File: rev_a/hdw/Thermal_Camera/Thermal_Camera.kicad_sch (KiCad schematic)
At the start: 0 parts

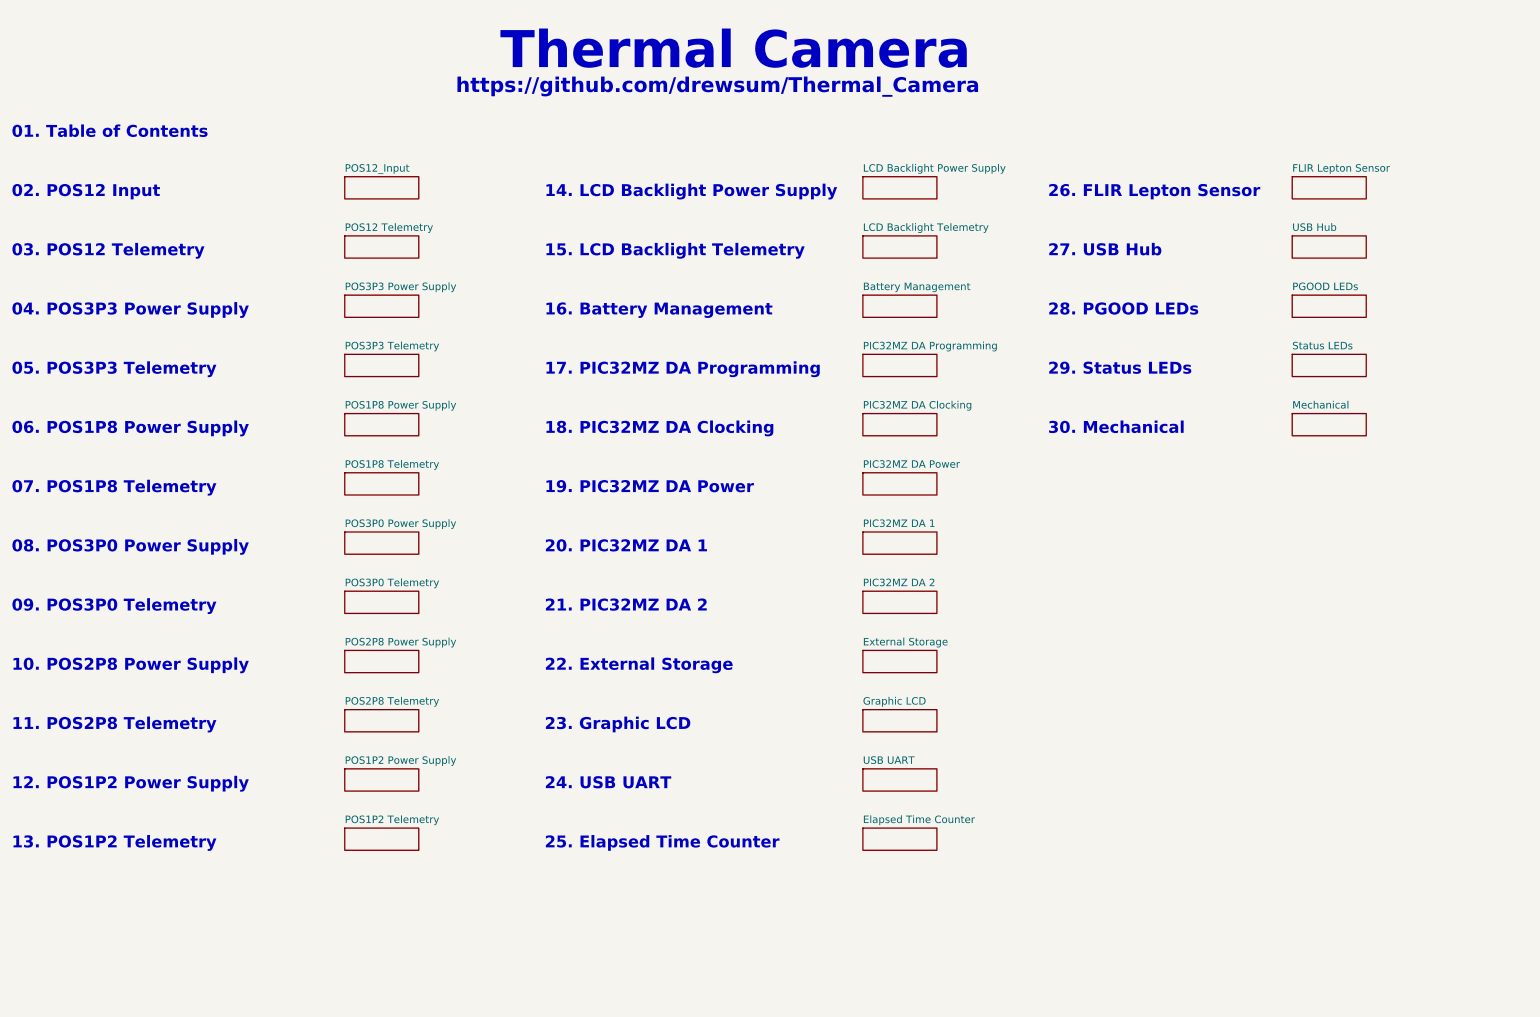
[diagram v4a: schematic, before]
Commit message: changed a lot of circuits from +3.3V to +3.0V VDD
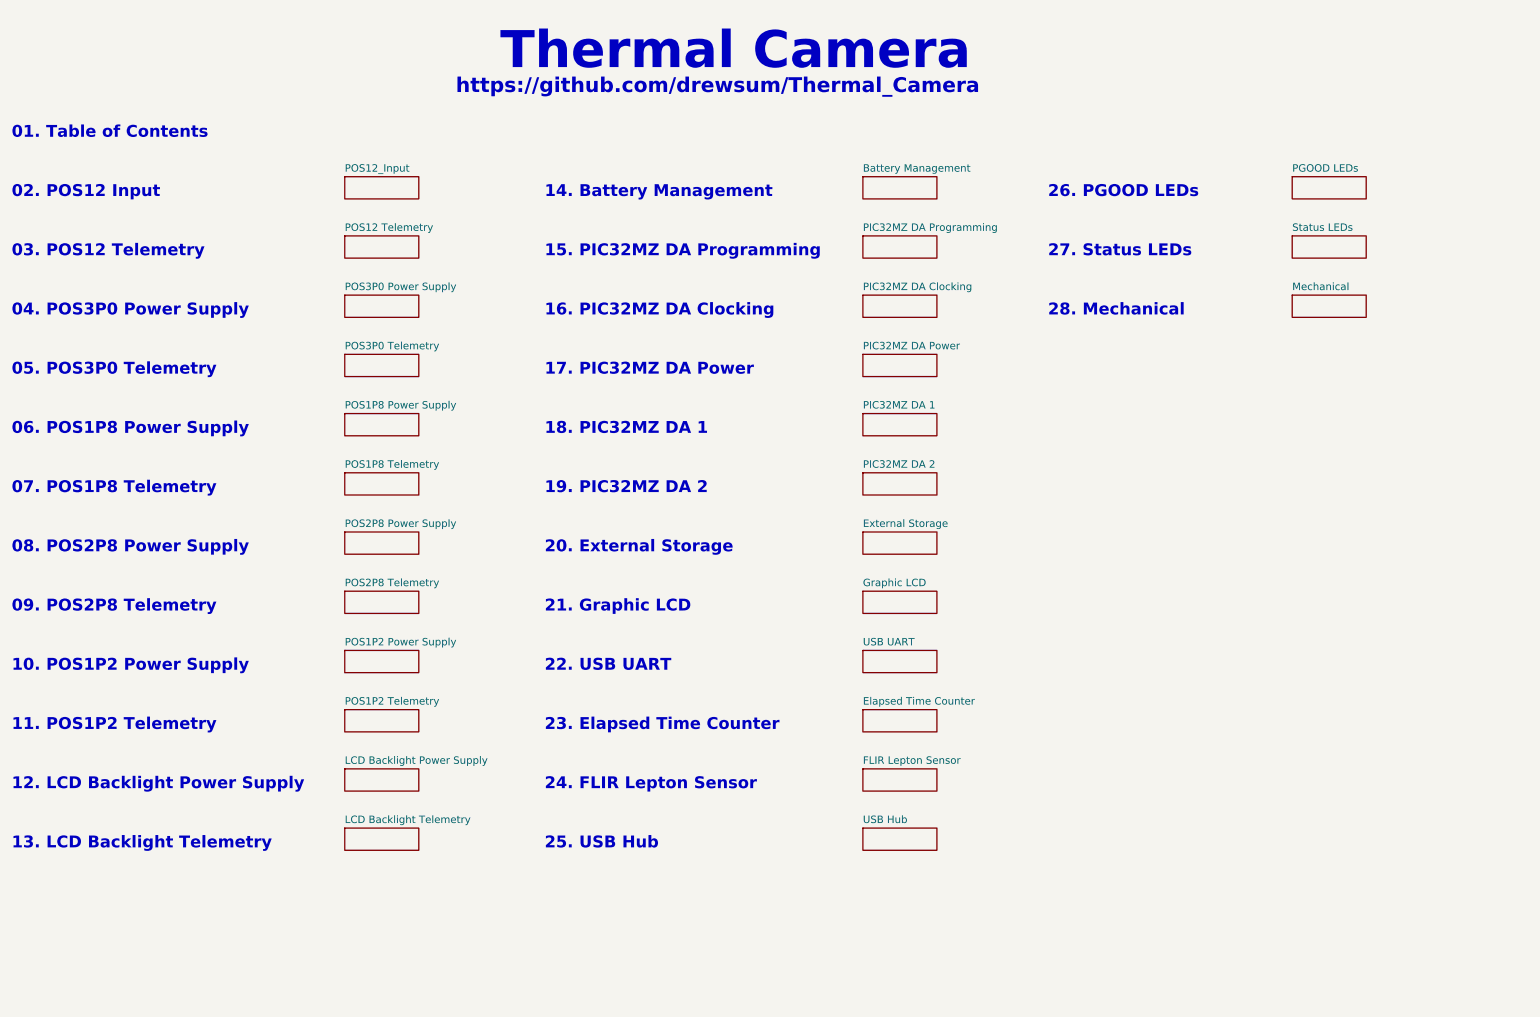
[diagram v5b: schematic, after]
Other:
- removed sheet POS3P3 Power Supply
- removed sheet POS3P3 Telemetry
- note added: "04. POS3P0 Power Supply"
- note added: "05. POS3P0 Telemetry"
- note added: "08. POS2P8 Power Supply"
- note added: "09. POS2P8 Telemetry"
- note added: "10. POS1P2 Power Supply"
- note added: "11. POS1P2 Telemetry"
- note added: "12. LCD Backlight Power Supply"
- note added: "13. LCD Backlight Telemetry"
- note added: "14. Battery Management"
- note added: "15. PIC32MZ DA Programming"
- note added: "16. PIC32MZ DA Clocking"
- note added: "17. PIC32MZ DA Power"
- note added: "18. PIC32MZ DA 1"
- note added: "19. PIC32MZ DA 2"
- note added: "20. External Storage"
- note added: "21. Graphic LCD"
- note added: "22. USB UART"
- note added: "23. Elapsed Time Counter"
- note added: "24. FLIR Lepton Sensor"
- note added: "25. USB Hub"
- note added: "26. PGOOD LEDs"
- note added: "27. Status LEDs"
- note added: "28. Mechanical"
- note removed: "04. POS3P3 Power Supply"
- note removed: "05. POS3P3 Telemetry"
- note removed: "08. POS3P0 Power Supply"
- note removed: "09. POS3P0 Telemetry"
- note removed: "10. POS2P8 Power Supply"
- note removed: "11. POS2P8 Telemetry"
- note removed: "12. POS1P2 Power Supply"
- note removed: "13. POS1P2 Telemetry"
- note removed: "14. LCD Backlight Power Supply"
- note removed: "15. LCD Backlight Telemetry"
- note removed: "16. Battery Management"
- note removed: "17. PIC32MZ DA Programming"
- note removed: "18. PIC32MZ DA Clocking"
- note removed: "19. PIC32MZ DA Power"
- note removed: "20. PIC32MZ DA 1"
- note removed: "21. PIC32MZ DA 2"
- note removed: "22. External Storage"
- note removed: "23. Graphic LCD"
- note removed: "24. USB UART"
- note removed: "25. Elapsed Time Counter"
- note removed: "26. FLIR Lepton Sensor"
- note removed: "27. USB Hub"
- note removed: "28. PGOOD LEDs"
- note removed: "29. Status LEDs"
- note removed: "30. Mechanical"

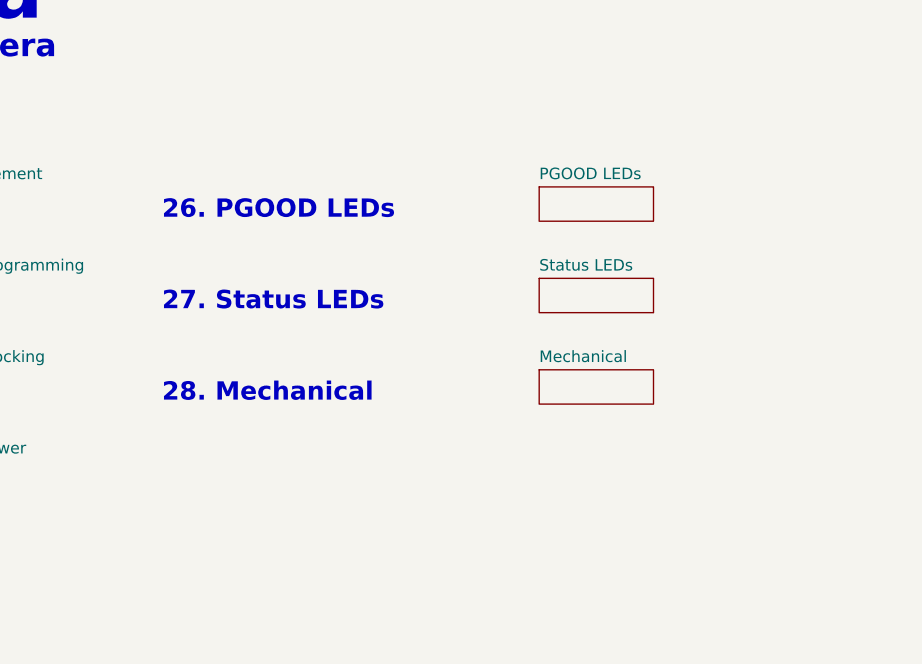
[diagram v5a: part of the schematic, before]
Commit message: added some USB stuff
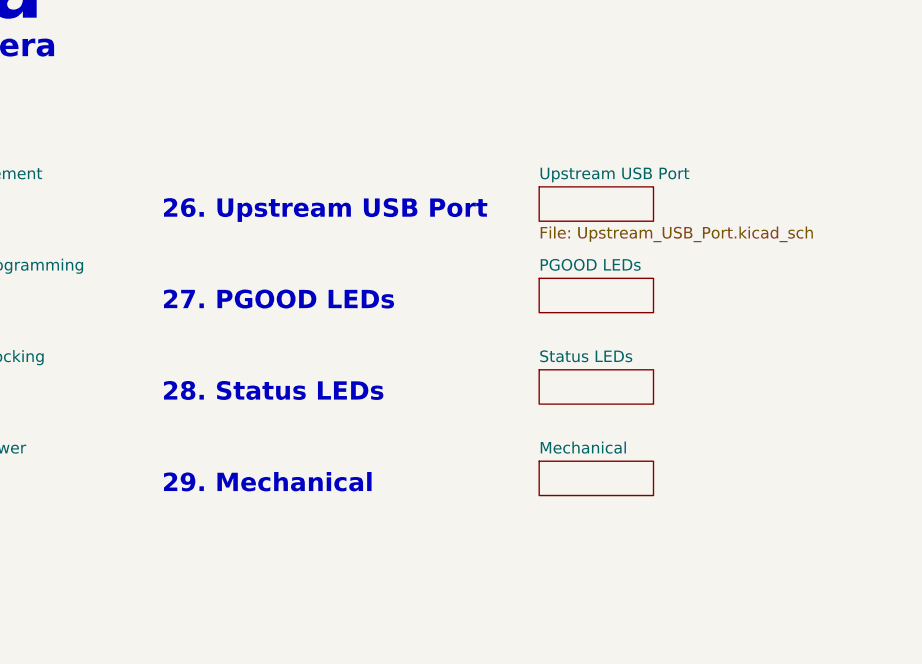
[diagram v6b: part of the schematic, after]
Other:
- added sheet Upstream USB Port (Upstream_USB_Port.kicad_sch)
- note added: "26. Upstream USB Port"
- note added: "27. PGOOD LEDs"
- note added: "28. Status LEDs"
- note added: "29. Mechanical"
- note removed: "26. PGOOD LEDs"
- note removed: "27. Status LEDs"
- note removed: "28. Mechanical"

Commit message: blah blah
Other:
- note added: "Add capacitive touch"
